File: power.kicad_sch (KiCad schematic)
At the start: 54 parts, among them U10 MAX4495AAUT, U11 MAX4495AAUT, U4 TPSM828302ARDSR, U5 LP3962EMP-3.3/NOPB, U6 STWD100NYWY3F, U8 MP5073GG-P, U9 MAX4495AAUT

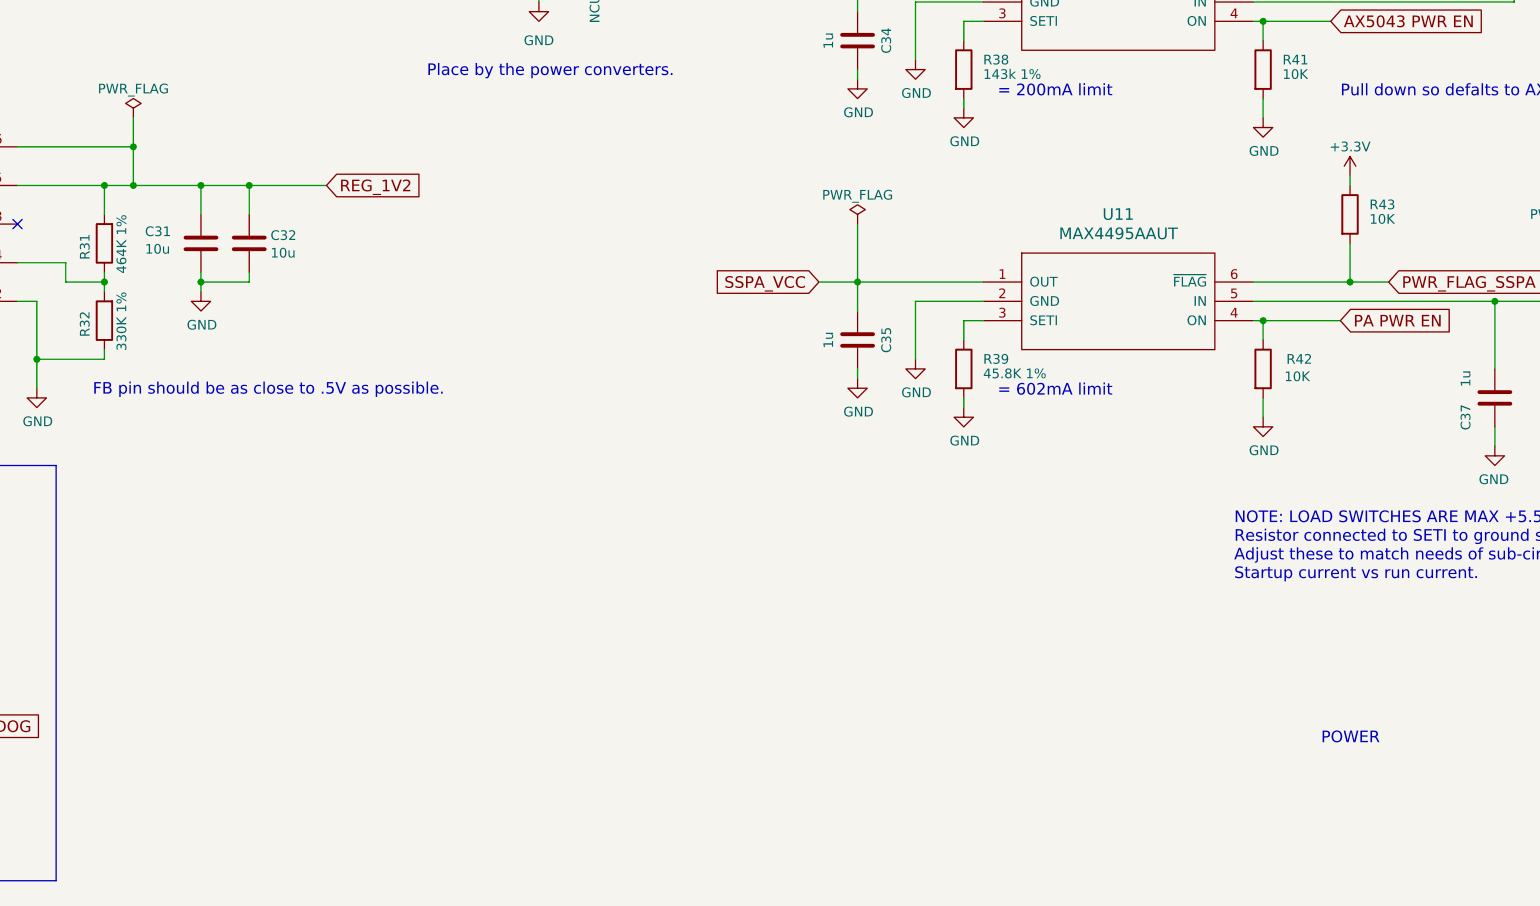
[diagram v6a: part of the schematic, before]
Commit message: Add 4 more MRAM parts
Signed-off-by: Corey Minyard <corey@minyard.net>
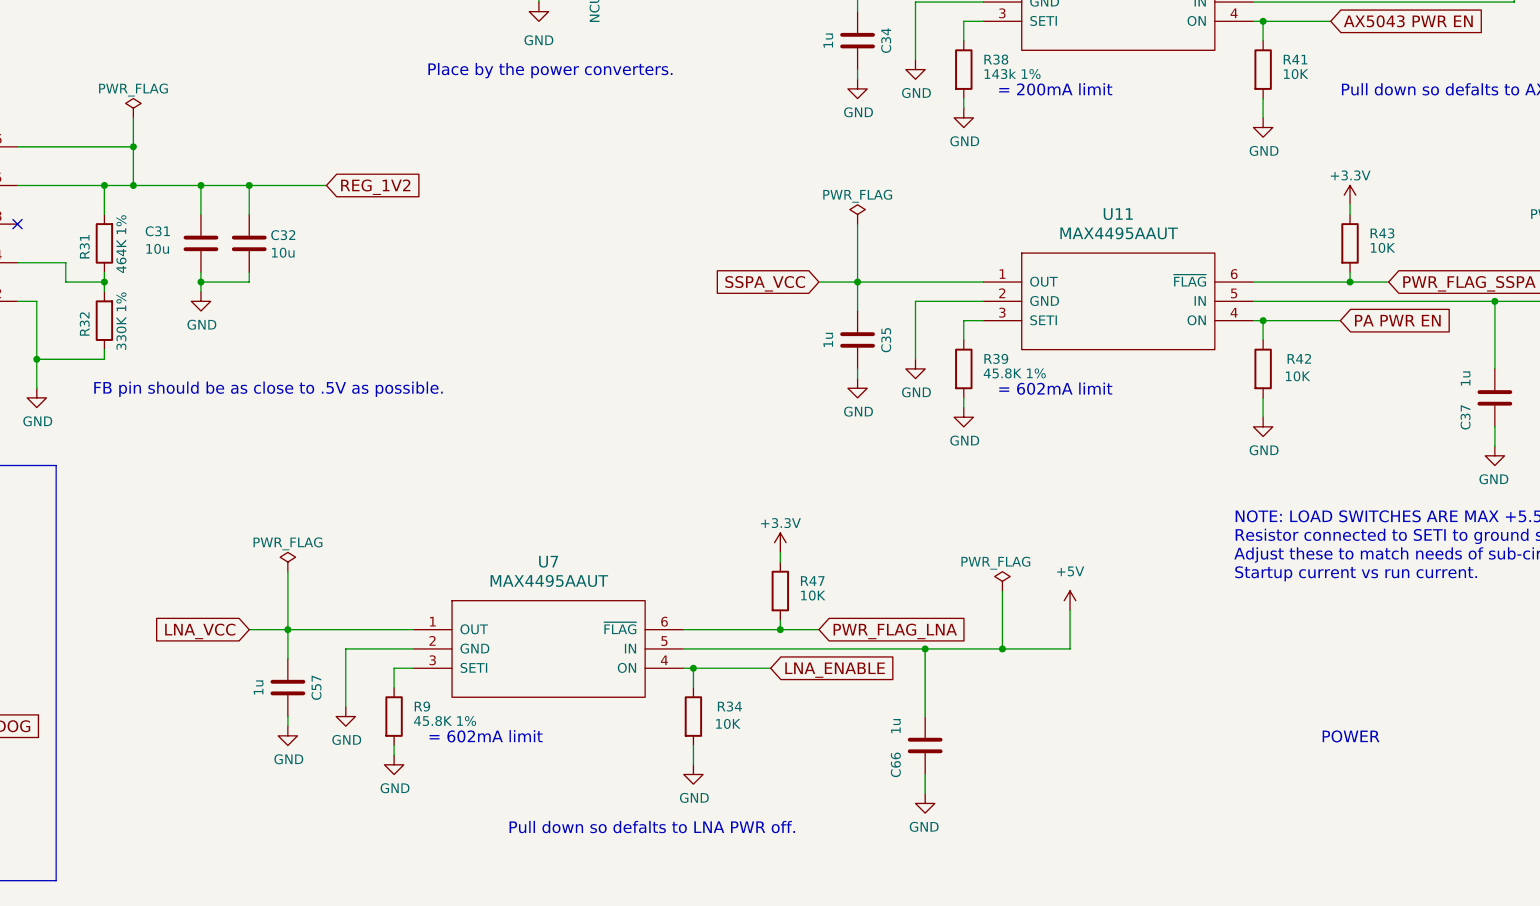
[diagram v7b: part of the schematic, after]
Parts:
- added C57, C66: 1u, Capacitor_SMD:C_0805_2012Metric_Pad1.18x1.45mm_HandSolder, symbol Device:C
- added R34, R47: 10K, Resistor_SMD:R_0603_1608Metric_Pad0.98x0.95mm_HandSolder, symbol Device:R
- added R9: 45.8K 1%, Resistor_SMD:R_0603_1608Metric_Pad0.98x0.95mm_HandSolder, symbol Device:R
- added U7: MAX4495AAUT, Package_TO_SOT_SMD:SOT-23-6_Handsoldering, symbol PACSAT_ICs:MAX4995AAUT
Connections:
- net +3.3V: now also R47.1
- net +5V: now also C66.1, U7.5 (IN)
- net GND: now also C57.2, C66.2, R34.2, R9.2, U7.2 (GND)
- new net: R9.1, U7.3 (SETI)
- new net LNA_ENABLE: R34.1, U7.4 (ON)
- new net LNA_VCC: C57.1, U7.1 (OUT)
- new net PWR_FLAG_LNA: R47.2, U7.6 (~{FLAG})
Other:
- note added: "Pull down so defalts to LNA PWR off."
- moved on the sheet: R43

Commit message: More work on various things
Signed-off-by: Corey Minyard <corey@minyard.net>
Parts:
- R9: value 45.8K 1% -> 143k 1%
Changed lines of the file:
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@@
 		)
 	)
-	(text "= 602mA limit"
+	(text "FIXME: DETERMINE REAL-WORLD LOAD AND MARGIN"
 		(exclude_from_sim no)
-		(at 216.535 245.11 0)
+		(at 294.64 123.825 0)
 		(effects
 			(font
@@
 		)
 	)
-	(text "FIXME: DETERMINE REAL-WORLD LOAD AND MARGIN"
+	(text ".1ms soft-start time"
 		(exclude_from_sim no)
-		(at 294.64 123.825 0)
+		(at 301.752 61.976 0)
 		(effects
 			(font
 				(size 1.524 1.524)
 			)
-			(justify left bottom)
 		)
 	)
-	(text ".1ms soft-start time"
+	(text "= 200mA limit"
 		(exclude_from_sim no)
-		(at 301.752 61.976 0)
+		(at 216.535 245.11 0)
 		(effects
 			(font
 				(size 1.524 1.524)
 			)
+			(justify left bottom)
 		)
 	)
@@
 	(symbol
 		(lib_id "Device:R")
-		(at 212.09 241.3 0)
-		(unit 1)
-		(exclude_from_sim no)
-		(in_bom yes)
-		(on_board yes)
-		(dnp no)
-		(property "Reference" "R9"
-			(at 214.63 240.03 0)
-			(effects
-				(font
-					(size 1.27 1.27)
-				)
-				(justify left)
-			)
-		)
-		(property "Value" "45.8K 1%"
-			(at 214.63 241.935 0)
-			(effects
-				(font
-					(size 1.27 1.27)
-				)
-				(justify left)
-			)
-		)
-		(property "Footprint" "Resistor_SMD:R_0603_1608Metric_Pad0.98x0.95mm_HandSolder"
-			(at 210.312 241.3 90)
-			(effects
-				(font
-					(size 1.27 1.27)
-				)
-				(hide yes)
-			)
-		)
-		(property "Datasheet" "~"
-			(at 212.09 241.3 0)
-			(effects
-				(font
-					(size 1.27 1.27)
-				)
-			)
-		)
-		(property "Description" ""
-			(at 212.09 241.3 0)
-			(effects
-				(font
-					(size 1.27 1.27)
-				)
-			)
-		)
-		(pin "1"
-		)
-		(pin "2"
-		)
-		(instances
-			(project "PacSat_AFSK"
-				(path "/cc9f42d2-6985-41ac-acab-5ab7b01c5b38/00000000-0000-0000-0000-00005a0ea76a"
-					(reference "R9")
-					(unit 1)
-				)
-			)
-		)
-	)
-	(symbol
-		(lib_id "Device:R")
 		(at 173.99 179.07 180)
 		(unit 1)
@@
 					(unit 1)
 				)
+			)
+		)
+	)
+	(symbol
+		(lib_id "Device:R")
+		(at 212.09 241.3 0)
+		(unit 1)
+		(exclude_from_sim no)
+		(in_bom yes)
+		(on_board yes)
+		(dnp no)
+		(property "Reference" "R9"
+			(at 214.63 240.03 0)
+			(effects
+				(font
+					(size 1.27 1.27)
+				)
+				(justify left)
+			)
+		)
+		(property "Value" "143k 1%"
+			(at 214.63 241.935 0)
+			(effects
+				(font
+					(size 1.27 1.27)
+				)
+				(justify left)
+			)
+		)
+		(property "Footprint" "Resistor_SMD:R_0603_1608Metric_Pad0.98x0.95mm_HandSolder"
+			(at 210.312 241.3 90)
+			(effects
+				(font
+					(size 1.27 1.27)
+				)
+				(hide yes)
+			)
+		)
+		(property "Datasheet" "~"
+			(at 212.09 241.3 0)
+			(effects
+				(font
+					(size 1.27 1.27)
+				)
+			)
+		)
+		(property "Description" ""
+			(at 212.09 241.3 0)
+			(effects
+				(font
+					(size 1.27 1.27)
+				)
+			)
+		)
+		(pin "1"
+		)
+		(pin "2"
+		)
+		(instances
+			(project "PacSat_AFSK"
+				(path "/cc9f42d2-6985-41ac-acab-5ab7b01c5b38/00000000-0000-0000-0000-00005a0ea76a"
+					(reference "R9")
+					(unit 1)
+				)
